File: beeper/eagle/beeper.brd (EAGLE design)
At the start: 29.2 x 39.8 mm, 32 parts, among them J4 ICSP, Q1 16MHz, T1 3904, U1 ATA6631, U2 ATMEGA328P

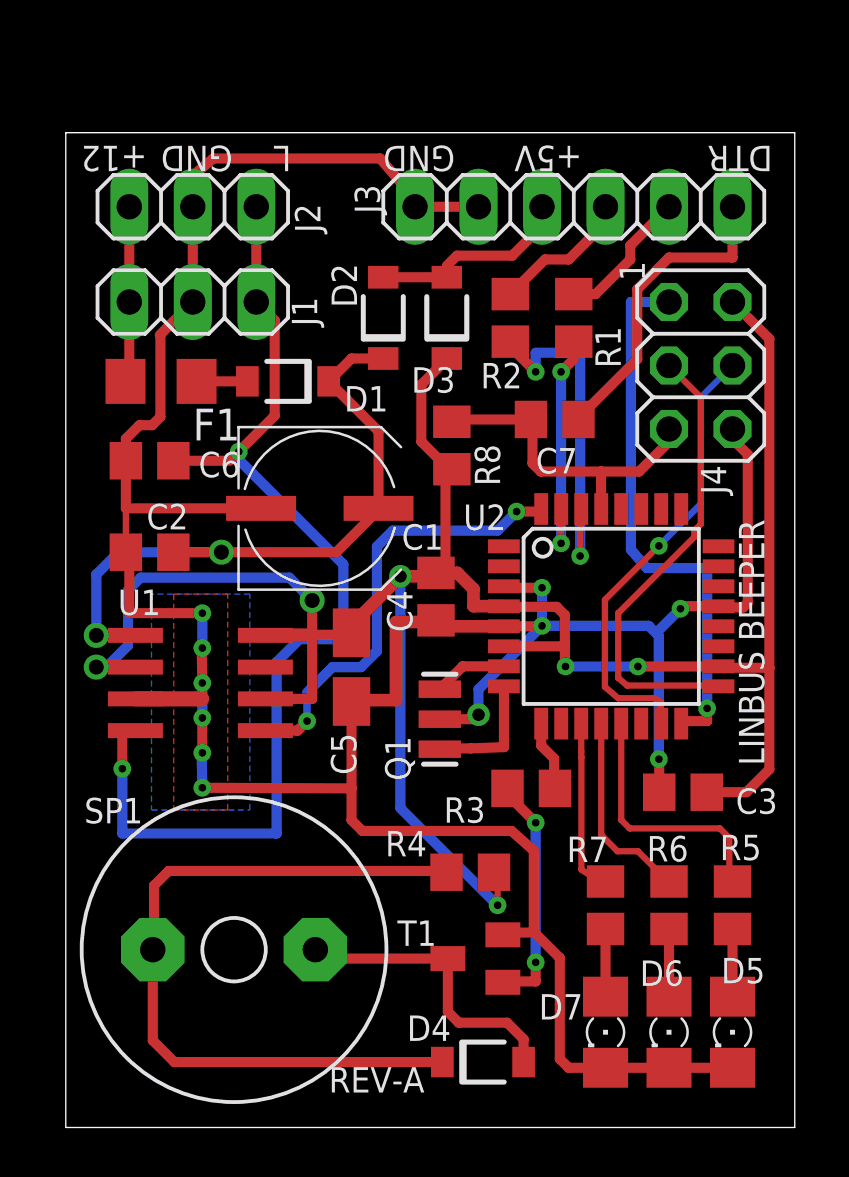
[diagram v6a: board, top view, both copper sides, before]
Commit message: Made the pads of the resonator longer for easy soldering. Tweaked the layout.
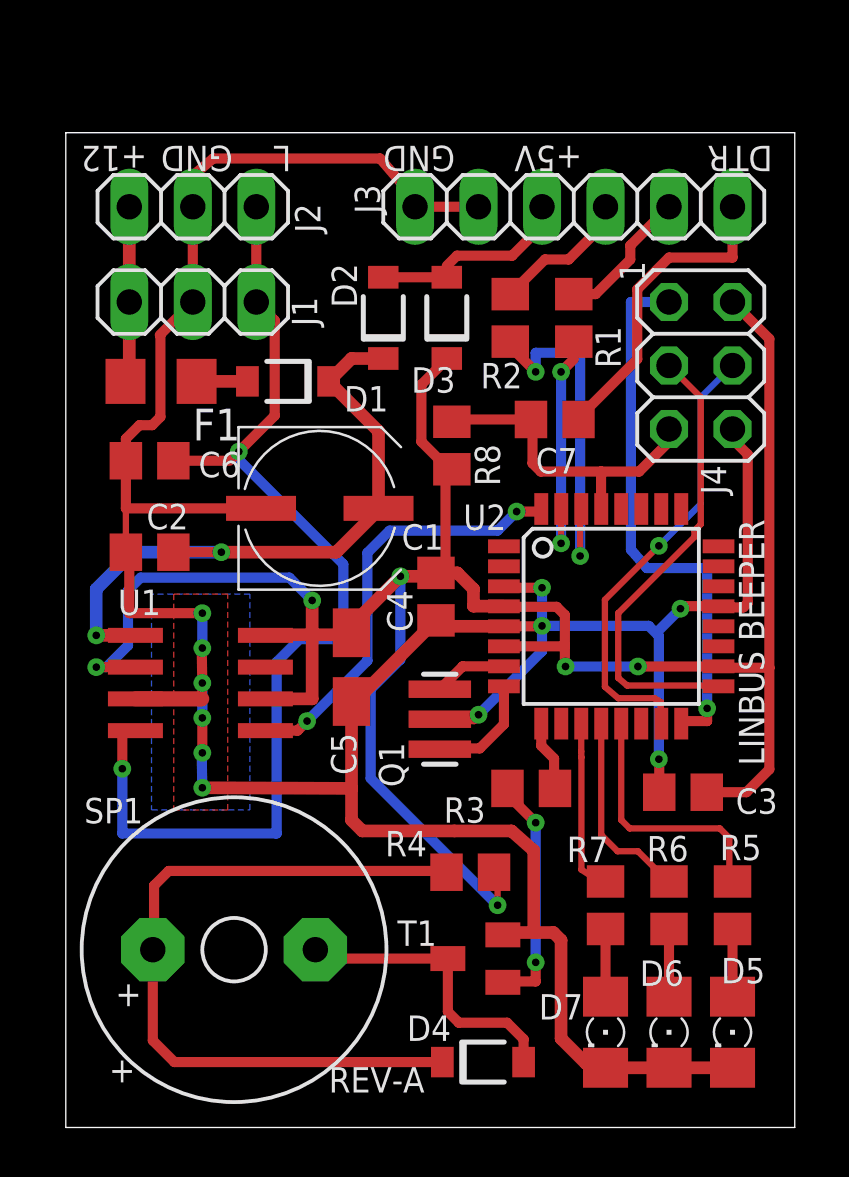
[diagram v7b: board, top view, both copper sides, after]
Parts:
- Q1: device SparkFun:RESONATOR-SMD -> beeper:RESONATOR-SMD
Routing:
- net GND: track 131.0 -> 129.1 mm
- net +5V: track 96.4 -> 97.4 mm
- net LIN_RX: track 17.8 -> 17.2 mm
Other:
- board text added: "+"
